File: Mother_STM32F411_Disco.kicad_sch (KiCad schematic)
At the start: 29 parts, among them U1 ESP32-DEVKIT-V1

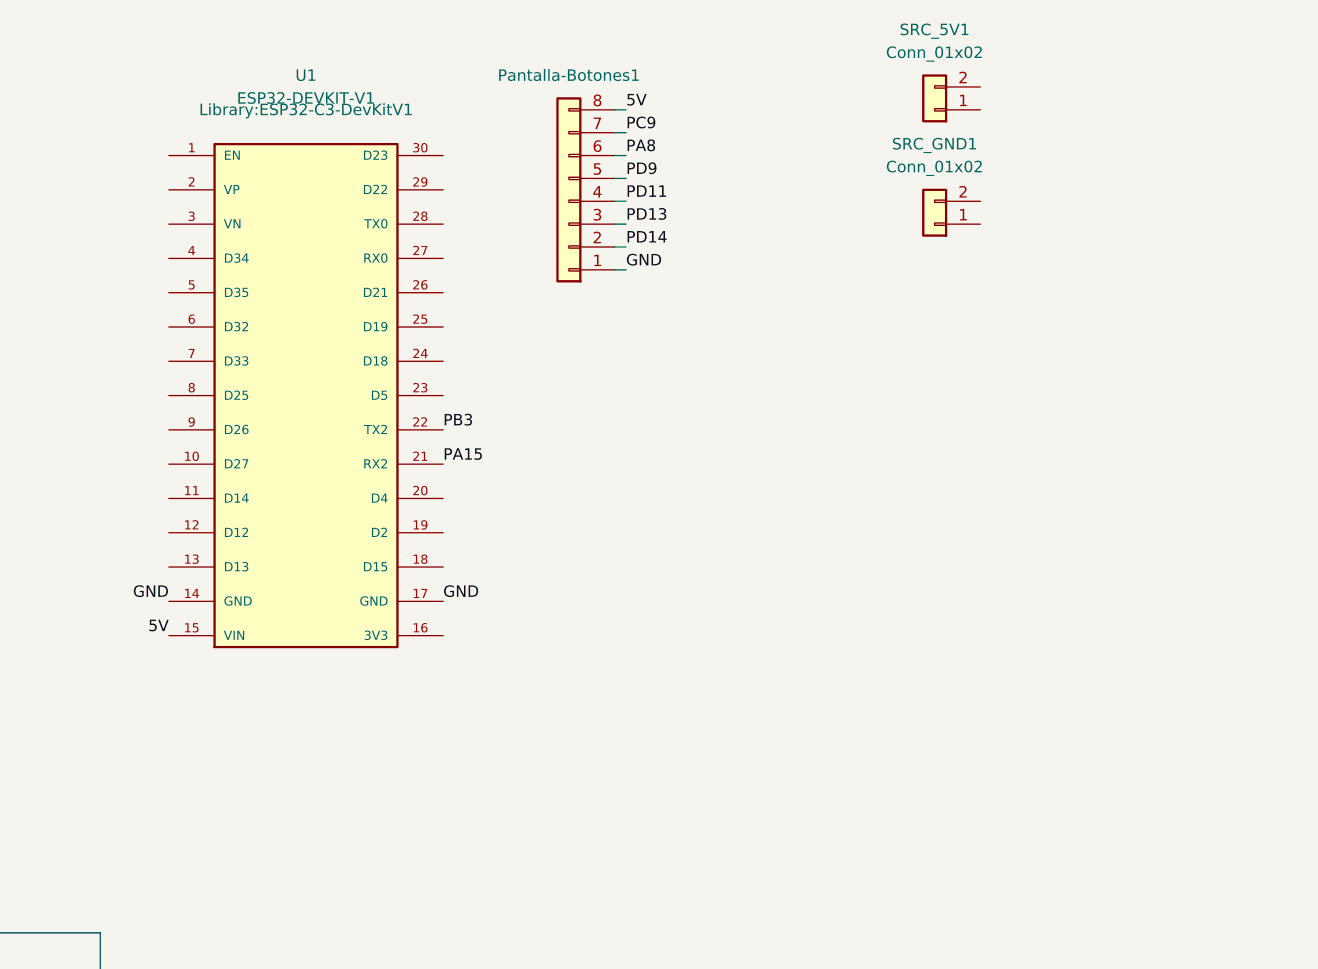
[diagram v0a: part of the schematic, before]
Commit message: Merge con master y agregamos filtros src
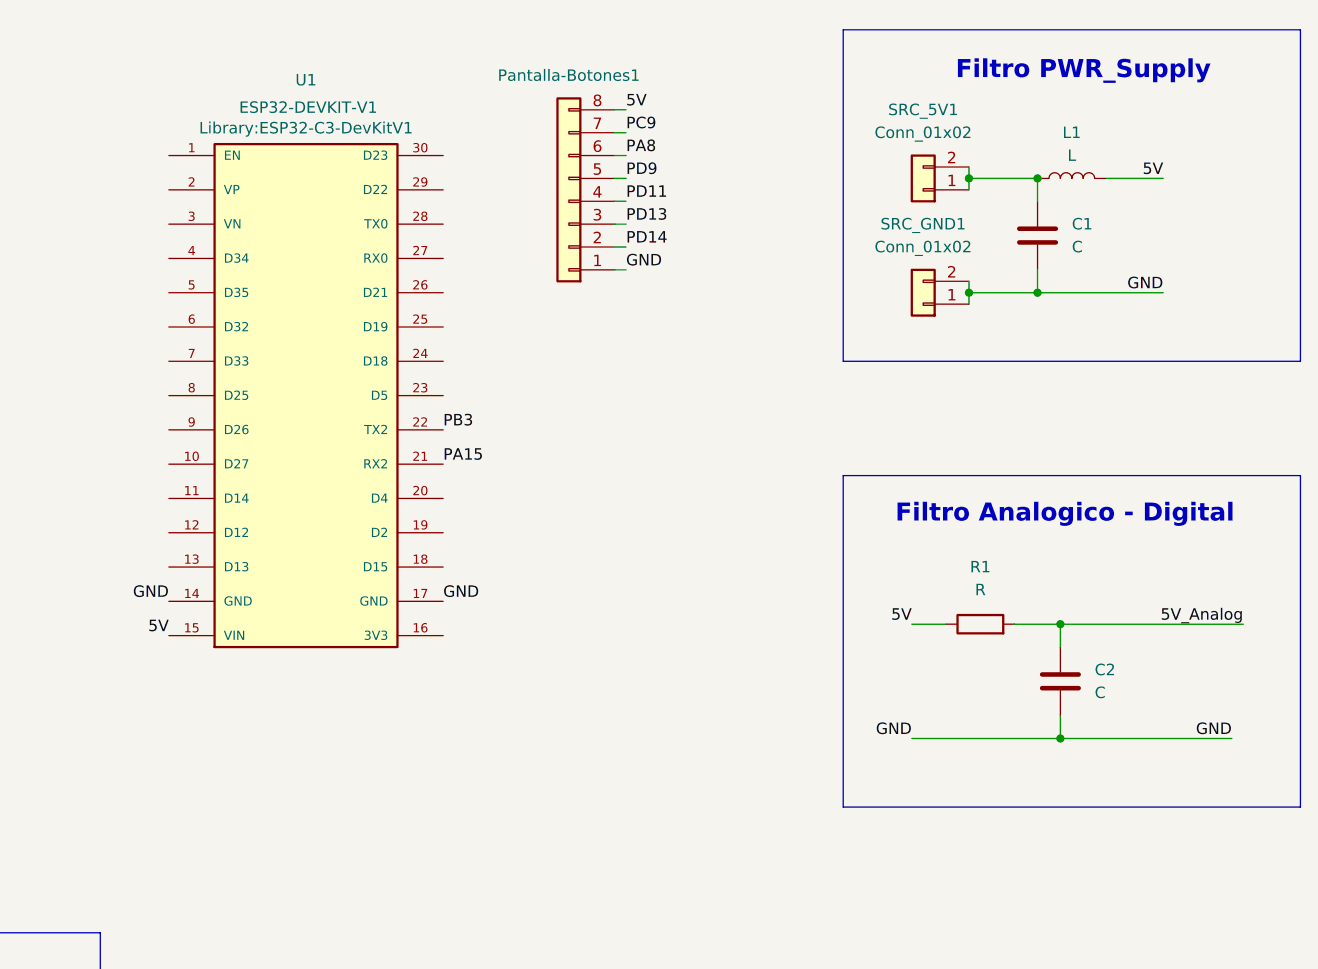
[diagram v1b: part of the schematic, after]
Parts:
- added C1, C2: C, symbol Device:C
- added L1: L, symbol Device:L
- added R1: R, symbol Device:R
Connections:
- net 5V: now also L1.2, R1.1
- net GND: now also SRC_GND1.1 (Pin_1), SRC_GND1.2 (Pin_2), C1.2, C2.2
- net at SRC_5V1.1 (Pin_1): now also SRC_5V1.2 (Pin_2), C1.1, L1.1
- new net 5V_Analog: C2.1, R1.2
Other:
- note added: "Filtro Analogico - Digital"
- note added: "Filtro PWR_Supply"
- moved on the sheet: SRC_5V1, SRC_GND1

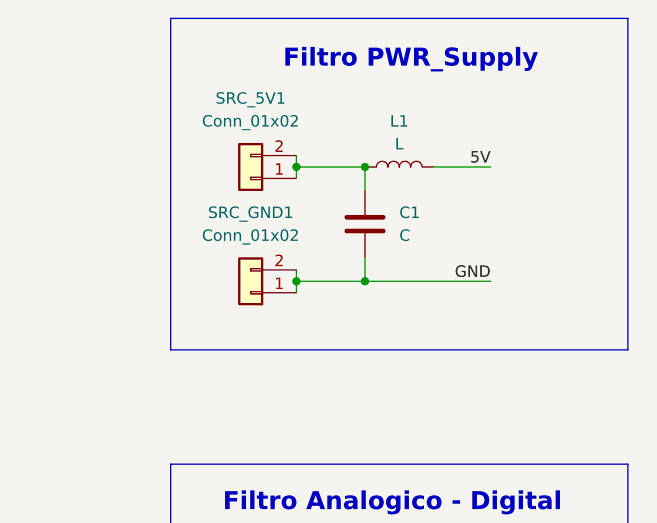
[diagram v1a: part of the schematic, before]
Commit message: Huellas placas check, falta huellas filtros
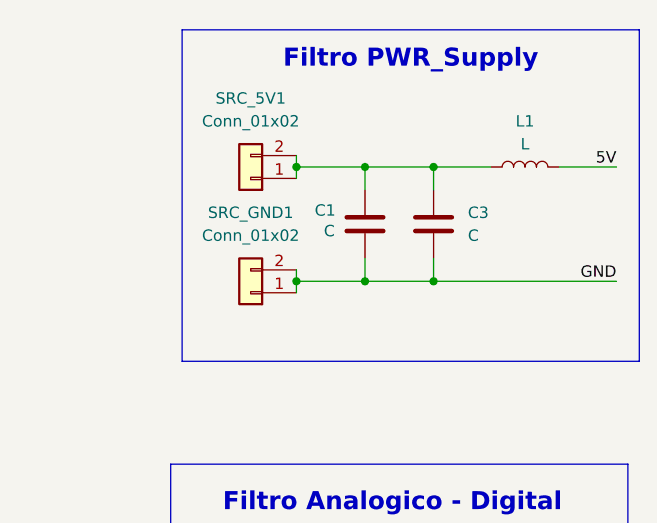
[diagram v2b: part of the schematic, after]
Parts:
- added C3: C, Capacitor_THT:C_Disc_D8.0mm_W5.0mm_P5.00mm, symbol Device:C
- C1: footprint (none) -> Capacitor_THT:CP_Radial_D13.0mm_P5.00mm
- C2: footprint (none) -> Capacitor_SMD:C_0805_2012Metric_Pad1.18x1.45mm_HandSolder
- L1: footprint (none) -> Inductor_THT:Choke_Schaffner_RN102-04-14.0x14.0mm
- R1: footprint (none) -> Resistor_SMD:R_0805_2012Metric_Pad1.20x1.40mm_HandSolder
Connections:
- net GND: now also C3.2
- net at C1.1, L1.1, SRC_5V1.1 (Pin_1)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: now also C3.1
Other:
- moved on the sheet: L1
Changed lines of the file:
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@@
 	)
 	(rectangle
-		(start 212.09 26.67)
-		(end 262.89 63.5)
+		(start 213.36 27.94)
+		(end 264.16 64.77)
 		(stroke
 			(width 0)
@@
 	)
 	(junction
+		(at 241.3 43.18)
+		(diameter 0)
+		(color 0 0 0 0)
+	)
+	(junction
 		(at 226.06 55.88)
 		(diameter 0)
@@
 	)
 	(junction
+		(at 241.3 55.88)
+		(diameter 0)
+		(color 0 0 0 0)
+	)
+	(junction
 		(at 236.22 105.41)
 		(diameter 0)
@@
 	(wire
 		(pts
+			(xy 241.3 53.34) (xy 241.3 55.88)
+		)
+		(stroke
+			(width 0)
+			(type default)
+		)
+	)
+	(wire
+		(pts
 			(xy 187.96 43.18) (xy 186.69 43.18)
 		)
@@
 	(wire
 		(pts
+			(xy 241.3 43.18) (xy 241.3 45.72)
+		)
+		(stroke
+			(width 0)
+			(type default)
+		)
+	)
+	(wire
+		(pts
 			(xy 76.2 52.07) (xy 80.01 52.07)
 		)
@@
 	(wire
 		(pts
+			(xy 241.3 55.88) (xy 261.62 55.88)
+		)
+		(stroke
+			(width 0)
+			(type default)
+		)
+	)
+	(wire
+		(pts
 			(xy 76.2 77.47) (xy 80.01 77.47)
 		)
@@
 	(wire
 		(pts
-			(xy 241.3 43.18) (xy 247.65 43.18)
+			(xy 255.27 43.18) (xy 261.62 43.18)
 		)
 		(stroke
@@
 	(wire
 		(pts
+			(xy 241.3 43.18) (xy 233.68 43.18)
+		)
+		(stroke
+			(width 0)
+			(type default)
+		)
+	)
+	(wire
+		(pts
 			(xy 236.22 105.41) (xy 255.27 105.41)
 		)
@@
 	(wire
 		(pts
-			(xy 233.68 55.88) (xy 247.65 55.88)
+			(xy 233.68 55.88) (xy 241.3 55.88)
 		)
 		(stroke
@@
 	(wire
 		(pts
+			(xy 247.65 43.18) (xy 241.3 43.18)
+		)
+		(stroke
+			(width 0)
+			(type default)
+		)
+	)
+	(wire
+		(pts
 			(xy 125.73 177.8) (xy 134.62 177.8)
 		)
@@
 	)
 	(label "5V"
-		(at 247.65 43.18 180)
+		(at 261.62 43.18 180)
 		(effects
 			(font
@@
 	)
 	(label "GND"
-		(at 247.65 55.88 180)
+		(at 261.62 55.88 180)
 		(effects
 			(font
@@
 		(on_board yes)
 		(dnp no)
-		(fields_autoplaced yes)
 		(property "Reference" "C1"
-			(at 237.49 48.2599 0)
+			(at 228.092 48.006 0)
 			(effects
 				(font
@@
 		)
 		(property "Value" "C"
-			(at 237.49 50.7999 0)
+			(at 229.108 50.292 0)
 			(effects
 				(font
@@
 			)
 		)
-		(property "Footprint" ""
+		(property "Footprint" "Capacitor_THT:CP_Radial_D13.0mm_P5.00mm"
 			(at 234.6452 53.34 0)
 			(effects
@@
 			)
 		)
-		(property "Footprint" ""
+		(property "Footprint" "Resistor_SMD:R_0805_2012Metric_Pad1.20x1.40mm_HandSolder"
 			(at 227.33 94.488 90)
 			(effects
@@
 			)
 		)
-		(property "Footprint" ""
+		(property "Footprint" "Capacitor_SMD:C_0805_2012Metric_Pad1.18x1.45mm_HandSolder"
 			(at 237.1852 102.87 0)
 			(effects
@@
 	)
 	(symbol
+		(lib_id "Device:C")
+		(at 241.3 49.53 0)
+		(unit 1)
+		(exclude_from_sim no)
+		(in_bom yes)
+		(on_board yes)
+		(dnp no)
+		(fields_autoplaced yes)
+		(property "Reference" "C3"
+			(at 245.11 48.2599 0)
+			(effects
+				(font
+					(size 1.27 1.27)
+				)
+				(justify left)
+			)
+		)
+		(property "Value" "C"
+			(at 245.11 50.7999 0)
+			(effects
+				(font
+					(size 1.27 1.27)
+				)
+				(justify left)
+			)
+		)
+		(property "Footprint" "Capacitor_THT:C_Disc_D8.0mm_W5.0mm_P5.00mm"
+			(at 242.2652 53.34 0)
+			(effects
+				(font
+					(size 1.27 1.27)
+				)
+				(hide yes)
+			)
+		)
+		(property "Datasheet" "~"
+			(at 241.3 49.53 0)
+			(effects
+				(font
+					(size 1.27 1.27)
+				)
+				(hide yes)
+			)
+		)
+		(property "Description" "Unpolarized capacitor"
+			(at 241.3 49.53 0)
+			(effects
+				(font
+					(size 1.27 1.27)
+				)
+				(hide yes)
+			)
+		)
+		(pin "2"
+		)
+		(pin "1"
+		)
+		(instances
+			(project "Mother_STM32F411_Disco"
+				(path "/a39c1df0-9e3d-4c83-b910-4e288e398b9e"
+					(reference "C3")
+					(unit 1)
+				)
+			)
+		)
+	)
+	(symbol
 		(lib_id "Connector_Generic:Conn_01x02")
 		(at 87.63 142.24 0)
@@
 	(symbol
 		(lib_id "Device:L")
-		(at 237.49 43.18 90)
+		(at 251.46 43.18 90)
 		(unit 1)
 		(exclude_from_sim no)
@@
 		(fields_autoplaced yes)
 		(property "Reference" "L1"
-			(at 237.49 38.1 90)
+			(at 251.46 38.1 90)
 			(effects
 				(font
@@
 		)
 		(property "Value" "L"
-			(at 237.49 40.64 90)
+			(at 251.46 40.64 90)
 			(effects
 				(font
@@
 			)
 		)
-		(property "Footprint" ""
-			(at 237.49 43.18 0)
+		(property "Footprint" "Inductor_THT:Choke_Schaffner_RN102-04-14.0x14.0mm"
+			(at 251.46 43.18 0)
 			(effects
 				(font
@@
 		)
 		(property "Datasheet" "~"
-			(at 237.49 43.18 0)
+			(at 251.46 43.18 0)
 			(effects
 				(font
@@
 		)
 		(property "Description" "Inductor"
-			(at 237.49 43.18 0)
+			(at 251.46 43.18 0)
 			(effects
 				(font

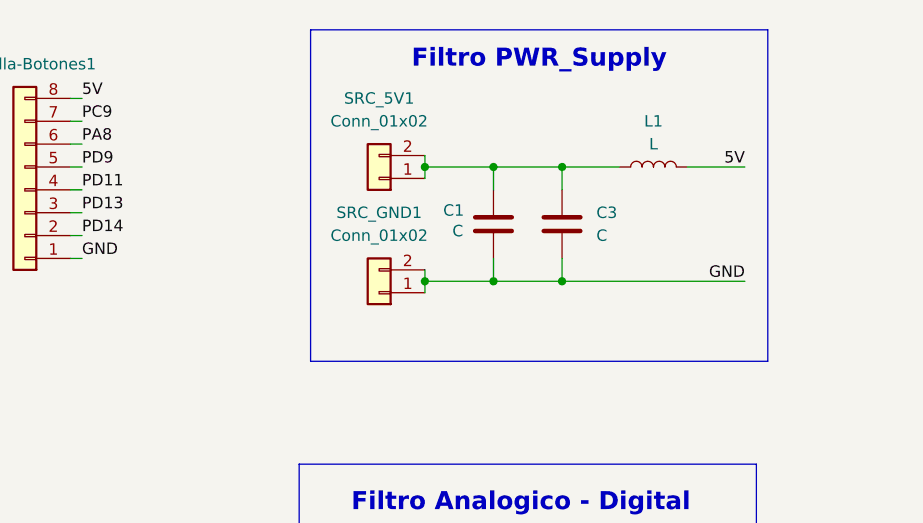
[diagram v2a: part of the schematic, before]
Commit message: fixed tamaño placa SRC_Supply
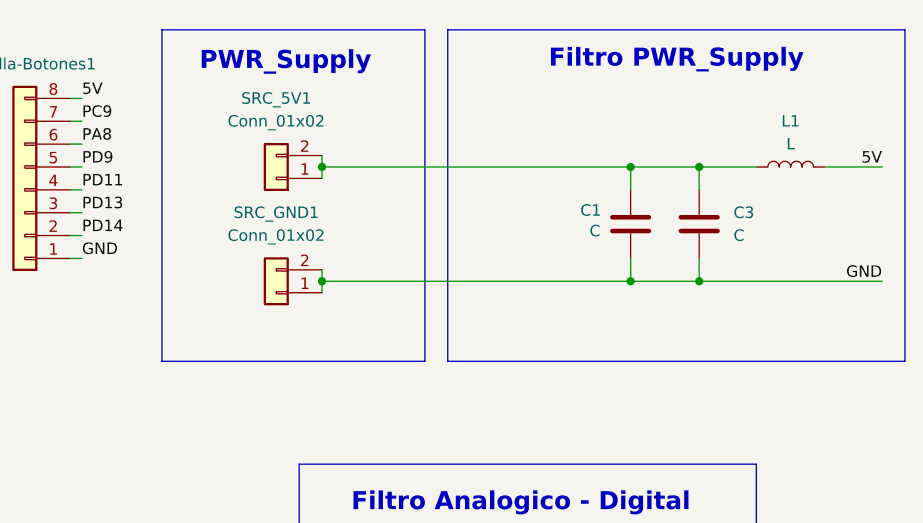
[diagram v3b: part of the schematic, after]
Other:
- note added: "PWR_Supply"
- moved on the sheet: C1, C3, L1, SRC_5V1, SRC_GND1
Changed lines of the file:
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@@
 	(paper "A4")
 	(rectangle
+		(start 196.85 27.94)
+		(end 226.06 64.77)
+		(stroke
+			(width 0)
+			(type solid)
+			(color 255 255 255 1)
+		)
+		(fill
+			(type color)
+			(color 255 0 255 0.4)
+		)
+	)
+	(rectangle
 		(start 78.74 127)
 		(end 129.54 147.32)
@@
 	)
 	(rectangle
-		(start 213.36 27.94)
-		(end 264.16 64.77)
+		(start 228.6 27.94)
+		(end 279.4 64.77)
 		(stroke
 			(width 0)
@@
 		)
 	)
+	(text "PWR_Supply\n"
+		(exclude_from_sim no)
+		(at 210.566 31.496 0)
+		(effects
+			(font
+				(size 2 2)
+				(thickness 0.4)
+				(bold yes)
+			)
+		)
+	)
 	(text "PAM8403 - 3\n"
 		(exclude_from_sim no)
@@
 	(text "Filtro PWR_Supply"
 		(exclude_from_sim no)
-		(at 238.76 31.242 0)
+		(at 254 31.242 0)
 		(effects
 			(font
@@
 	)
 	(junction
-		(at 233.68 43.18)
+		(at 248.92 43.18)
 		(diameter 0)
 		(color 0 0 0 0)
 	)
 	(junction
-		(at 241.3 43.18)
+		(at 214.63 43.18)
 		(diameter 0)
 		(color 0 0 0 0)
 	)
 	(junction
-		(at 226.06 55.88)
+		(at 256.54 43.18)
 		(diameter 0)
 		(color 0 0 0 0)
 	)
 	(junction
-		(at 226.06 43.18)
+		(at 214.63 55.88)
 		(diameter 0)
 		(color 0 0 0 0)
 	)
 	(junction
-		(at 233.68 55.88)
+		(at 248.92 55.88)
 		(diameter 0)
 		(color 0 0 0 0)
 	)
 	(junction
-		(at 241.3 55.88)
+		(at 256.54 55.88)
 		(diameter 0)
 		(color 0 0 0 0)
@@
 	(wire
 		(pts
-			(xy 226.06 43.18) (xy 226.06 44.45)
+			(xy 214.63 43.18) (xy 214.63 44.45)
 		)
 		(stroke
@@
 	(wire
 		(pts
-			(xy 226.06 41.91) (xy 226.06 43.18)
+			(xy 214.63 41.91) (xy 214.63 43.18)
 		)
 		(stroke
@@
 	(wire
 		(pts
-			(xy 233.68 53.34) (xy 233.68 55.88)
+			(xy 248.92 53.34) (xy 248.92 55.88)
 		)
 		(stroke
@@
 	(wire
 		(pts
+			(xy 214.63 43.18) (xy 248.92 43.18)
+		)
+		(stroke
+			(width 0)
+			(type default)
+		)
+	)
+	(wire
+		(pts
 			(xy 77.47 166.37) (xy 82.55 166.37)
 		)
@@
 	(wire
 		(pts
-			(xy 226.06 54.61) (xy 226.06 55.88)
+			(xy 214.63 54.61) (xy 214.63 55.88)
 		)
 		(stroke
@@
 	(wire
 		(pts
+			(xy 214.63 55.88) (xy 248.92 55.88)
+		)
+		(stroke
+			(width 0)
+			(type default)
+		)
+	)
+	(wire
+		(pts
 			(xy 125.73 135.89) (xy 134.62 135.89)
 		)
@@
 	(wire
 		(pts
-			(xy 241.3 53.34) (xy 241.3 55.88)
+			(xy 256.54 53.34) (xy 256.54 55.88)
 		)
 		(stroke
@@
 	(wire
 		(pts
-			(xy 233.68 43.18) (xy 226.06 43.18)
-		)
-		(stroke
-			(width 0)
-			(type default)
-		)
-	)
-	(wire
-		(pts
 			(xy 187.96 38.1) (xy 186.69 38.1)
 		)
@@
 	(wire
 		(pts
-			(xy 241.3 43.18) (xy 241.3 45.72)
+			(xy 256.54 43.18) (xy 256.54 45.72)
 		)
 		(stroke
@@
 	(wire
 		(pts
-			(xy 241.3 55.88) (xy 261.62 55.88)
+			(xy 256.54 55.88) (xy 276.86 55.88)
 		)
 		(stroke
@@
 	(wire
 		(pts
-			(xy 226.06 55.88) (xy 226.06 57.15)
+			(xy 214.63 55.88) (xy 214.63 57.15)
 		)
 		(stroke
@@
 	(wire
 		(pts
-			(xy 255.27 43.18) (xy 261.62 43.18)
+			(xy 270.51 43.18) (xy 276.86 43.18)
 		)
 		(stroke
@@
 	(wire
 		(pts
-			(xy 241.3 43.18) (xy 233.68 43.18)
+			(xy 256.54 43.18) (xy 248.92 43.18)
 		)
 		(stroke
@@
 	(wire
 		(pts
-			(xy 233.68 55.88) (xy 241.3 55.88)
+			(xy 248.92 55.88) (xy 256.54 55.88)
 		)
 		(stroke
@@
 	(wire
 		(pts
-			(xy 233.68 45.72) (xy 233.68 43.18)
+			(xy 248.92 45.72) (xy 248.92 43.18)
 		)
 		(stroke
@@
 	(wire
 		(pts
-			(xy 247.65 43.18) (xy 241.3 43.18)
+			(xy 262.89 43.18) (xy 256.54 43.18)
 		)
 		(stroke
@@
 	(wire
 		(pts
-			(xy 226.06 55.88) (xy 233.68 55.88)
-		)
-		(stroke
-			(width 0)
-			(type default)
-		)
-	)
-	(wire
-		(pts
 			(xy 82.55 161.29) (xy 62.23 161.29)
 		)
@@
 	)
 	(label "5V"
-		(at 261.62 43.18 180)
+		(at 276.86 43.18 180)
 		(effects
 			(font
@@
 	)
 	(label "GND"
-		(at 261.62 55.88 180)
+		(at 276.86 55.88 180)
 		(effects
 			(font
@@
 	(symbol
 		(lib_id "Connector_Generic:Conn_01x02")
-		(at 220.98 44.45 180)
+		(at 209.55 44.45 180)
 		(unit 1)
 		(exclude_from_sim no)
@@
 		(fields_autoplaced yes)
 		(property "Reference" "SRC_5V1"
-			(at 220.98 35.56 0)
+			(at 209.55 35.56 0)
 			(effects
 				(font
@@
 		)
 		(property "Value" "Conn_01x02"
-			(at 220.98 38.1 0)
+			(at 209.55 38.1 0)
 			(effects
 				(font
@@
 		)
 		(property "Footprint" "Connector_PinSocket_2.54mm:PinSocket_1x02_P2.54mm_Vertical"
-			(at 220.98 44.45 0)
+			(at 209.55 44.45 0)
 			(effects
 				(font
@@
 		)
 		(property "Datasheet" "~"
-			(at 220.98 44.45 0)
+			(at 209.55 44.45 0)
 			(effects
 				(font
@@
 		)
 		(property "Description" "Generic connector, single row, 01x02, script generated (kicad-library-utils/schlib/autogen/connector/)"
-			(at 220.98 44.45 0)
+			(at 209.55 44.45 0)
 			(effects
 				(font
@@
 	(symbol
 		(lib_id "Device:C")
-		(at 233.68 49.53 0)
+		(at 248.92 49.53 0)
 		(unit 1)
 		(exclude_from_sim no)
@@
 		(dnp no)
 		(property "Reference" "C1"
-			(at 228.092 48.006 0)
+			(at 243.332 48.006 0)
 			(effects
 				(font
@@
 		)
 		(property "Value" "C"
-			(at 229.108 50.292 0)
+			(at 244.348 50.292 0)
 			(effects
 				(font
@@
 		)
 		(property "Footprint" "Capacitor_THT:CP_Radial_D13.0mm_P5.00mm"
-			(at 234.6452 53.34 0)
+			(at 249.8852 53.34 0)
 			(effects
 				(font
@@
 		)
 		(property "Datasheet" "~"
-			(at 233.68 49.53 0)
+			(at 248.92 49.53 0)
 			(effects
 				(font
@@
 		)
 		(property "Description" "Unpolarized capacitor"
-			(at 233.68 49.53 0)
+			(at 248.92 49.53 0)
 			(effects
 				(font
@@
 	(symbol
 		(lib_id "Device:C")
-		(at 241.3 49.53 0)
+		(at 256.54 49.53 0)
 		(unit 1)
 		(exclude_from_sim no)
@@
 		(fields_autoplaced yes)
 		(property "Reference" "C3"
-			(at 245.11 48.2599 0)
+			(at 260.35 48.2599 0)
 			(effects
 				(font
@@
 		)
 		(property "Value" "C"
-			(at 245.11 50.7999 0)
+			(at 260.35 50.7999 0)
 			(effects
 				(font
@@
 		)
 		(property "Footprint" "Capacitor_THT:C_Disc_D8.0mm_W5.0mm_P5.00mm"
-			(at 242.2652 53.34 0)
+			(at 257.5052 53.34 0)
 			(effects
 				(font
@@
 		)
 		(property "Datasheet" "~"
-			(at 241.3 49.53 0)
+			(at 256.54 49.53 0)
 			(effects
 				(font
@@
 		)
 		(property "Description" "Unpolarized capacitor"
-			(at 241.3 49.53 0)
+			(at 256.54 49.53 0)
 			(effects
 				(font
@@
 	(symbol
 		(lib_id "Connector_Generic:Conn_01x02")
-		(at 220.98 57.15 180)
+		(at 209.55 57.15 180)
 		(unit 1)
 		(exclude_from_sim no)
@@
 		(fields_autoplaced yes)
 		(property "Reference" "SRC_GND1"
-			(at 220.98 48.26 0)
+			(at 209.55 48.26 0)
 			(effects
 				(font
@@
 		)
 		(property "Value" "Conn_01x02"
-			(at 220.98 50.8 0)
+			(at 209.55 50.8 0)
 			(effects
 				(font
@@
 		)
 		(property "Footprint" "Connector_PinSocket_2.54mm:PinSocket_1x02_P2.54mm_Vertical"
-			(at 220.98 57.15 0)
+			(at 209.55 57.15 0)
 			(effects
 				(font
@@
 		)
 		(property "Datasheet" "~"
-			(at 220.98 57.15 0)
+			(at 209.55 57.15 0)
 			(effects
 				(font
@@
 		)
 		(property "Description" "Generic connector, single row, 01x02, script generated (kicad-library-utils/schlib/autogen/connector/)"
-			(at 220.98 57.15 0)
+			(at 209.55 57.15 0)
 			(effects
 				(font
@@
 	(symbol
 		(lib_id "Device:L")
-		(at 251.46 43.18 90)
+		(at 266.7 43.18 90)
 		(unit 1)
 		(exclude_from_sim no)
@@
 		(fields_autoplaced yes)
 		(property "Reference" "L1"
-			(at 251.46 38.1 90)
+			(at 266.7 38.1 90)
 			(effects
 				(font
@@
 		)
 		(property "Value" "L"
-			(at 251.46 40.64 90)
+			(at 266.7 40.64 90)
 			(effects
 				(font
@@
 		)
 		(property "Footprint" "Inductor_THT:Choke_Schaffner_RN102-04-14.0x14.0mm"
-			(at 251.46 43.18 0)
+			(at 266.7 43.18 0)
 			(effects
 				(font
@@
 		)
 		(property "Datasheet" "~"
-			(at 251.46 43.18 0)
+			(at 266.7 43.18 0)
 			(effects
 				(font
@@
 		)
 		(property "Description" "Inductor"
-			(at 251.46 43.18 0)
+			(at 266.7 43.18 0)
 			(effects
 				(font
